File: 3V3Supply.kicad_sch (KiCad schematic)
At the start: 6 parts, among them U5 NCP163ASN330T1G

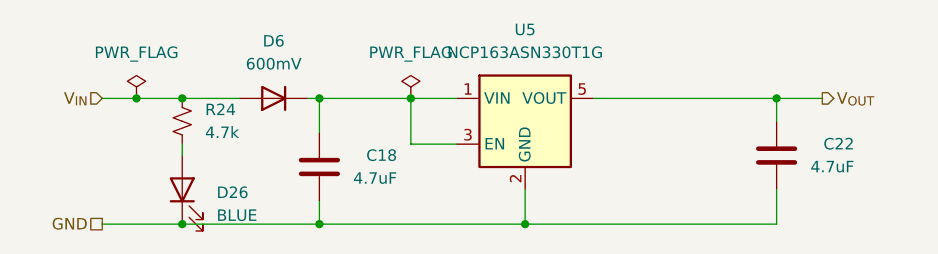
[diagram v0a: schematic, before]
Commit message: updated to external adc
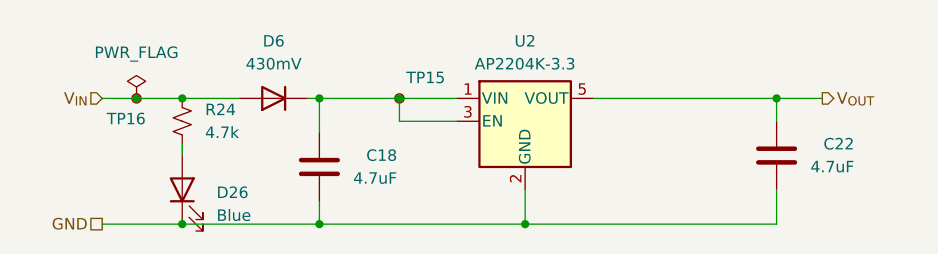
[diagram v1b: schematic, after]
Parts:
- removed U5: NCP163ASN330T1G, Package_TO_SOT_SMD:SOT-23-5, symbol Regulator_Linear:NCP163ASN330T1G
- added TP15, TP16: ${SHORT_NET_NAME(1)}, TestPoint:TestPoint_Pad_D1.0mm, symbol OpenMC:TestPoint_Small
- added U2: AP2204K-3.3, Package_TO_SOT_SMD:SOT-23-5, symbol Regulator_Linear:AP2204K-3.3
- C18, C22: symbol Device:C -> OpenMC:C; MPN (none) -> CC0603ZRY5V5BB475
- D26: value BLUE -> Blue; symbol Device:LED -> OpenMC:LED; MPN (none) -> VLMB1300-GS08
- D6: value 600mV -> 430mV; symbol Device:D -> OpenMC:D; MPN (none) -> CD0603-B0340R
- R24: symbol Device:R_Small_US -> OpenMC:R_Small_US; MPN (none) -> CR0603-FX-4701ELF
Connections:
- net GND: now also U2.2 (GND)
- net V_{IN}: now also TP16.1
- net V_{OUT}: now also U2.5 (VOUT)
- net at C18.1, D6.1 (K): now also TP15.1, U2.1 (VIN), U2.3 (EN)
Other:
- company: Nebula Labs -> (none)

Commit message: hello
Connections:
- net VIN: now reaches C18.1, D6.1 (K), TP15.1, U2.1 (VIN), U2.3 (EN)
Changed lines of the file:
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@@
+		)
+	)
+	(label "VIN"
+		(at 91.44 62.23 0)
+		(fields_autoplaced yes)
+		(effects
+			(font
+				(size 1.27 1.27)
+			)
+			(justify left bottom)
 		)
 	)
